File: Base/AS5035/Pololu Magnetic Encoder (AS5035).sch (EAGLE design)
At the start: 9 parts, among them U1 AS5035

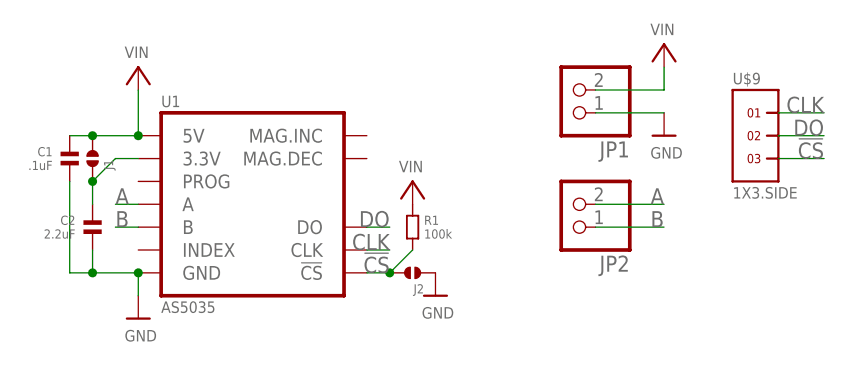
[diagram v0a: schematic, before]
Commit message: Cleaned up AS5035 based Magnetic Encoder. Added Silkscreen adn removed SPI components.
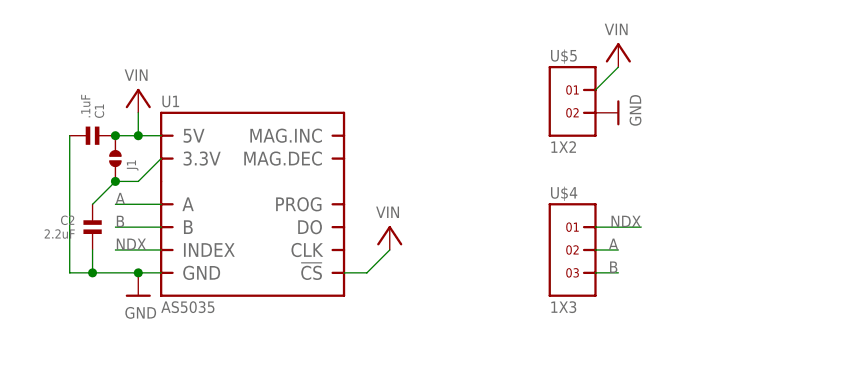
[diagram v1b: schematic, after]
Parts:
- removed J2: (no value), .solderjumper:SOLDERJUMPER.2.LRG.PASTE
- removed JP1, JP2: (no value), microbuilder:HEADER-1X2ROUND
- removed R1: 100k, .standardparts:RESISTOR.0603
- removed U$9: 1X3.SIDE, .standardheaders:1X3.SIDE
- added U$4: 1X3, headers(.1in):1X3
- added U$5: 1X2, headers(.1in):1X2
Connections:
- removed net !CS: J2.2, R1.2, U$9.3, U1.!CS
- removed net CLK: U$9.1, U1.CLK
- removed net DO: U$9.2, U1.DO
- new net NDX: U$4.1, U1.INDEX
- net A: now also U$4.2; no longer JP2.2
- net B: now also U$4.3; no longer JP2.1
- net GND: now also U$5.2; no longer J2.1, JP1.1
- net VIN: now also U$5.1, U1.!CS; no longer JP1.2, R1.1
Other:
- moved on the sheet: C1, J1
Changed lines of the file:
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@@
 <?xml version="1.0" encoding="utf-8"?>
 <!DOCTYPE eagle SYSTEM "eagle.dtd">
-<eagle version="6.3">
+<eagle version="6.4">
 <drawing>
 <settings>
@@
 <part name="U$2" library="microbuilder" deviceset="VIN" device=""/>
 <part name="U$3" library="microbuilder" deviceset="GND" device=""/>
-<part name="U$4" library="microbuilder" deviceset="GND" device=""/>
-<part name="J2" library=".solderjumper" deviceset="SOLDERJUMPER.2" device=".LRG.PASTE"/>
 <part name="U$7" library="microbuilder" deviceset="VIN" device=""/>
 <part name="U$8" library="microbuilder" deviceset="GND" device=""/>
-<part name="U$9" library=".standardheaders" deviceset="1X3" device=".SIDE"/>
 <part name="U$10" library="thinkmaketest" deviceset="A4_LAYOUT" device=""/>
-<part name="JP1" library="microbuilder" deviceset="HEADER-1X2" device="ROUND"/>
-<part name="JP2" library="microbuilder" deviceset="HEADER-1X2" device="ROUND"/>
-<part name="R1" library=".standardparts" deviceset="RESISTOR" device=".0603" value="100k"/>
 <part name="U$1" library="microbuilder" deviceset="VIN" device=""/>
+<part name="U$4" library="headers(.1in)" deviceset="1X3" device=""/>
+<part name="U$5" library="headers(.1in)" deviceset="1X2" device=""/>
 </parts>
 <sheets>
@@
 <instances>
 <instance part="U1" gate="G$1" x="38.1" y="142.24"/>
-<instance part="C1" gate="G$1" x="17.78" y="147.32" rot="MR270"/>
+<instance part="C1" gate="G$1" x="20.32" y="149.86" rot="MR0"/>
 <instance part="C2" gate="G$1" x="20.32" y="139.7" rot="MR270"/>
-<instance part="J1" gate="G$1" x="20.32" y="147.32" rot="MR90"/>
-<instance part="U$2" gate="G$1" x="25.4" y="154.94"/>
-<instance part="U$3" gate="G$1" x="25.4" y="129.54"/>
-<instance part="U$4" gate="G$1" x="58.42" y="132.08"/>
-<instance part="J2" gate="G$1" x="55.88" y="134.62" rot="R180"/>
-<instance part="U$7" gate="G$1" x="83.82" y="157.48"/>
-<instance part="U$8" gate="G$1" x="83.82" y="149.86"/>
-<instance part="U$9" gate="G$1" x="93.98" y="149.86"/>
+<instance part="J1" gate="G$1" x="22.86" y="147.32" rot="MR90"/>
+<instance part="U$2" gate="G$1" x="25.4" y="152.4"/>
+<instance part="U$3" gate="G$1" x="25.4" y="132.08"/>
+<instance part="U$7" gate="G$1" x="78.74" y="157.48"/>
+<instance part="U$8" gate="G$1" x="78.74" y="152.4" rot="R90"/>
 <instance part="U$10" gate="G$1" x="0" y="0"/>
-<instance part="JP1" gate="G$1" x="73.66" y="154.94" rot="R180"/>
-<instance part="JP2" gate="G$1" x="73.66" y="142.24" rot="R180"/>
-<instance part="R1" gate="G$1" x="55.88" y="139.7" rot="R270"/>
-<instance part="U$1" gate="G$1" x="55.88" y="142.24"/>
+<instance part="U$1" gate="G$1" x="53.34" y="137.16"/>
+<instance part="U$4" gate="G$1" x="73.66" y="137.16"/>
+<instance part="U$5" gate="G$1" x="73.66" y="154.94"/>
 </instances>
 <busses>
@@
 <pinref part="U1" gate="G$1" pin="5V"/>
 <pinref part="U$2" gate="G$1" pin="VIN"/>
-<wire x1="25.4" y1="149.86" x2="25.4" y2="154.94" width="0.1524" layer="91"/>
 <pinref part="C1" gate="G$1" pin="1"/>
+<pinref part="J1" gate="G$1" pin="2"/>
+<wire x1="22.86" y1="149.86" x2="25.4" y2="149.86" width="0.1524" layer="91"/>
+<junction x="22.86" y="149.86"/>
+<wire x1="25.4" y1="149.86" x2="27.94" y2="149.86" width="0.1524" layer="91"/>
+<wire x1="25.4" y1="149.86" x2="25.4" y2="152.4" width="0.1524" layer="91"/>
 <junction x="25.4" y="149.86"/>
-<wire x1="17.78" y1="149.86" x2="20.32" y2="149.86" width="0.1524" layer="91"/>
-<pinref part="J1" gate="G$1" pin="2"/>
-<wire x1="20.32" y1="149.86" x2="25.4" y2="149.86" width="0.1524" layer="91"/>
-<junction x="20.32" y="149.86"/>
 </segment>
 <segment>
 <pinref part="U$7" gate="G$1" pin="VIN"/>
-<wire x1="83.82" y1="154.94" x2="83.82" y2="157.48" width="0.1524" layer="91"/>
-<pinref part="JP1" gate="G$1" pin="2"/>
-<wire x1="76.2" y1="154.94" x2="83.82" y2="154.94" width="0.1524" layer="91"/>
-</segment>
-<segment>
-<pinref part="R1" gate="G$1" pin="1"/>
+<wire x1="76.2" y1="154.94" x2="78.74" y2="157.48" width="0.1524" layer="91"/>
+<pinref part="U$5" gate="G$1" pin="1"/>
+</segment>
+<segment>
+<pinref part="U1" gate="G$1" pin="!CS"/>
 <pinref part="U$1" gate="G$1" pin="VIN"/>
+<wire x1="48.26" y1="134.62" x2="50.8" y2="134.62" width="0.1524" layer="91"/>
+<wire x1="50.8" y1="134.62" x2="53.34" y2="137.16" width="0.1524" layer="91"/>
 </segment>
 </net>
@@
 <segment>
 <pinref part="U1" gate="G$1" pin="A"/>
-<wire x1="25.4" y1="142.24" x2="22.86" y2="142.24" width="0.1524" layer="91"/>
-<label x="22.86" y="142.24" size="1.778" layer="95"/>
-</segment>
-<segment>
-<pinref part="JP2" gate="G$1" pin="2"/>
-<wire x1="76.2" y1="142.24" x2="83.82" y2="142.24" width="0.1524" layer="91"/>
-<label x="83.82" y="142.24" size="1.778" layer="95" rot="MR0"/>
+<wire x1="27.94" y1="142.24" x2="22.86" y2="142.24" width="0.1524" layer="91"/>
+<label x="22.86" y="142.24" size="1.27" layer="95"/>
+</segment>
+<segment>
+<pinref part="U$4" gate="G$1" pin="2"/>
+<wire x1="78.74" y1="137.16" x2="76.2" y2="137.16" width="0.1524" layer="91"/>
+<label x="78.74" y="137.16" size="1.27" layer="95" rot="MR0"/>
 </segment>
 </net>
@@
 <segment>
 <pinref part="U1" gate="G$1" pin="B"/>
-<wire x1="22.86" y1="139.7" x2="25.4" y2="139.7" width="0.1524" layer="91"/>
-<label x="22.86" y="139.7" size="1.778" layer="95"/>
-</segment>
-<segment>
-<pinref part="JP2" gate="G$1" pin="1"/>
-<wire x1="83.82" y1="139.7" x2="76.2" y2="139.7" width="0.1524" layer="91"/>
-<label x="83.82" y="139.7" size="1.778" layer="95" rot="MR0"/>
+<wire x1="22.86" y1="139.7" x2="27.94" y2="139.7" width="0.1524" layer="91"/>
+<label x="22.86" y="139.7" size="1.27" layer="95"/>
+</segment>
+<segment>
+<pinref part="U$4" gate="G$1" pin="3"/>
+<wire x1="76.2" y1="134.62" x2="78.74" y2="134.62" width="0.1524" layer="91"/>
+<label x="78.74" y="134.62" size="1.27" layer="95" rot="MR0"/>
 </segment>
 </net>
@@
 <pinref part="U$3" gate="G$1" pin="GND"/>
 <pinref part="U1" gate="G$1" pin="GND"/>
-<wire x1="25.4" y1="132.08" x2="25.4" y2="134.62" width="0.1524" layer="91"/>
+<wire x1="27.94" y1="134.62" x2="25.4" y2="134.62" width="0.1524" layer="91"/>
+<pinref part="C2" gate="G$1" pin="2"/>
 <wire x1="25.4" y1="134.62" x2="20.32" y2="134.62" width="0.1524" layer="91"/>
-<junction x="25.4" y="134.62"/>
-<pinref part="C2" gate="G$1" pin="2"/>
 <wire x1="20.32" y1="134.62" x2="20.32" y2="137.16" width="0.1524" layer="91"/>
 <pinref part="C1" gate="G$1" pin="2"/>
-<wire x1="17.78" y1="144.78" x2="17.78" y2="134.62" width="0.1524" layer="91"/>
+<wire x1="17.78" y1="149.86" x2="17.78" y2="134.62" width="0.1524" layer="91"/>
 <wire x1="17.78" y1="134.62" x2="20.32" y2="134.62" width="0.1524" layer="91"/>
 <junction x="20.32" y="134.62"/>
-</segment>
-<segment>
-<pinref part="JP1" gate="G$1" pin="1"/>
-<wire x1="83.82" y1="152.4" x2="76.2" y2="152.4" width="0.1524" layer="91"/>
+<junction x="25.4" y="134.62"/>
+</segment>
+<segment>
 <pinref part="U$8" gate="G$1" pin="GND"/>
-</segment>
-<segment>
-<pinref part="J2" gate="G$1" pin="1"/>
-<pinref part="U$4" gate="G$1" pin="GND"/>
-</segment>
-</net>
-<net name="!CS" class="0">
-<segment>
-<pinref part="U$9" gate="G$1" pin="3"/>
-<wire x1="96.52" y1="147.32" x2="101.6" y2="147.32" width="0.1524" layer="91"/>
-<label x="101.6" y="147.32" size="1.778" layer="95" rot="MR0"/>
-</segment>
-<segment>
-<pinref part="J2" gate="G$1" pin="2"/>
-<pinref part="U1" gate="G$1" pin="!CS"/>
-<wire x1="53.34" y1="134.62" x2="50.8" y2="134.62" width="0.1524" layer="91"/>
-<wire x1="53.34" y1="134.62" x2="55.88" y2="137.16" width="0.1524" layer="91"/>
-<junction x="53.34" y="134.62"/>
-<pinref part="R1" gate="G$1" pin="2"/>
-<label x="53.34" y="134.62" size="1.778" layer="95" rot="MR0"/>
-</segment>
-</net>
-<net name="CLK" class="0">
-<segment>
-<pinref part="U1" gate="G$1" pin="CLK"/>
-<wire x1="50.8" y1="137.16" x2="53.34" y2="137.16" width="0.1524" layer="91"/>
-<label x="53.34" y="137.16" size="1.778" layer="95" rot="MR0"/>
-</segment>
-<segment>
-<pinref part="U$9" gate="G$1" pin="1"/>
-<wire x1="96.52" y1="152.4" x2="101.6" y2="152.4" width="0.1524" layer="91"/>
-<label x="101.6" y="152.4" size="1.778" layer="95" rot="MR0"/>
-</segment>
-</net>
-<net name="DO" class="0">
-<segment>
-<pinref part="U1" gate="G$1" pin="DO"/>
-<wire x1="50.8" y1="139.7" x2="53.34" y2="139.7" width="0.1524" layer="91"/>
-<label x="53.34" y="139.7" size="1.778" layer="95" rot="MR0"/>
-</segment>
-<segment>
-<pinref part="U$9" gate="G$1" pin="2"/>
-<wire x1="96.52" y1="149.86" x2="101.6" y2="149.86" width="0.1524" layer="91"/>
-<label x="101.6" y="149.86" size="1.778" layer="95" rot="MR0"/>
+<pinref part="U$5" gate="G$1" pin="2"/>
 </segment>
 </net>
@@
 <pinref part="C2" gate="G$1" pin="1"/>
 <pinref part="J1" gate="G$1" pin="1"/>
-<wire x1="20.32" y1="144.78" x2="20.32" y2="142.24" width="0.1524" layer="91"/>
+<wire x1="22.86" y1="144.78" x2="20.32" y2="142.24" width="0.1524" layer="91"/>
 <pinref part="U1" gate="G$1" pin="3.3V"/>
-<wire x1="20.32" y1="144.78" x2="22.86" y2="147.32" width="0.1524" layer="91"/>
-<wire x1="22.86" y1="147.32" x2="25.4" y2="147.32" width="0.1524" layer="91"/>
-<junction x="20.32" y="144.78"/>
-</segment>
-</net>
+<wire x1="22.86" y1="144.78" x2="25.4" y2="144.78" width="0.1524" layer="91"/>
+<wire x1="25.4" y1="144.78" x2="27.94" y2="147.32" width="0.1524" layer="91"/>
+<junction x="22.86" y="144.78"/>
+</segment>
+</net>
+<net name="NDX" class="0">
+<segment>
+<pinref part="U1" gate="G$1" pin="INDEX"/>
+<wire x1="27.94" y1="137.16" x2="22.86" y2="137.16" width="0.1524" layer="91"/>
+<label x="22.86" y="137.16" size="1.27" layer="95"/>
+</segment>
+<segment>
+<pinref part="U$4" gate="G$1" pin="1"/>
+<wire x1="76.2" y1="139.7" x2="81.28" y2="139.7" width="0.1524" layer="91"/>
+<label x="81.28" y="139.7" size="1.27" layer="95" rot="MR0"/>
+</segment>
+</net>

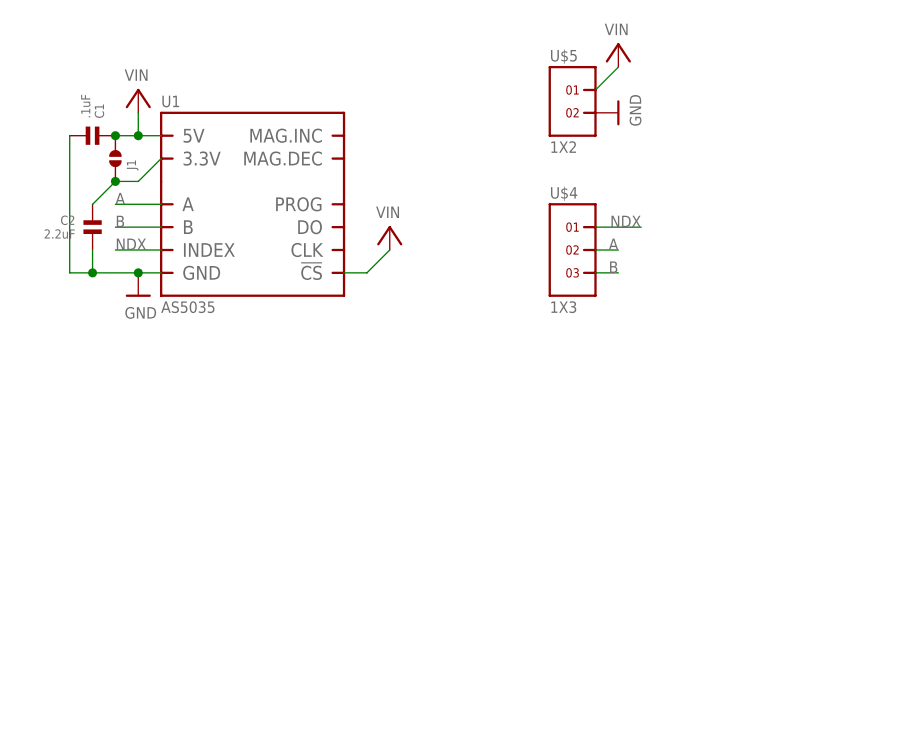
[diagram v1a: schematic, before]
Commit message: CS should be tied low for QEI to work on the AS5035
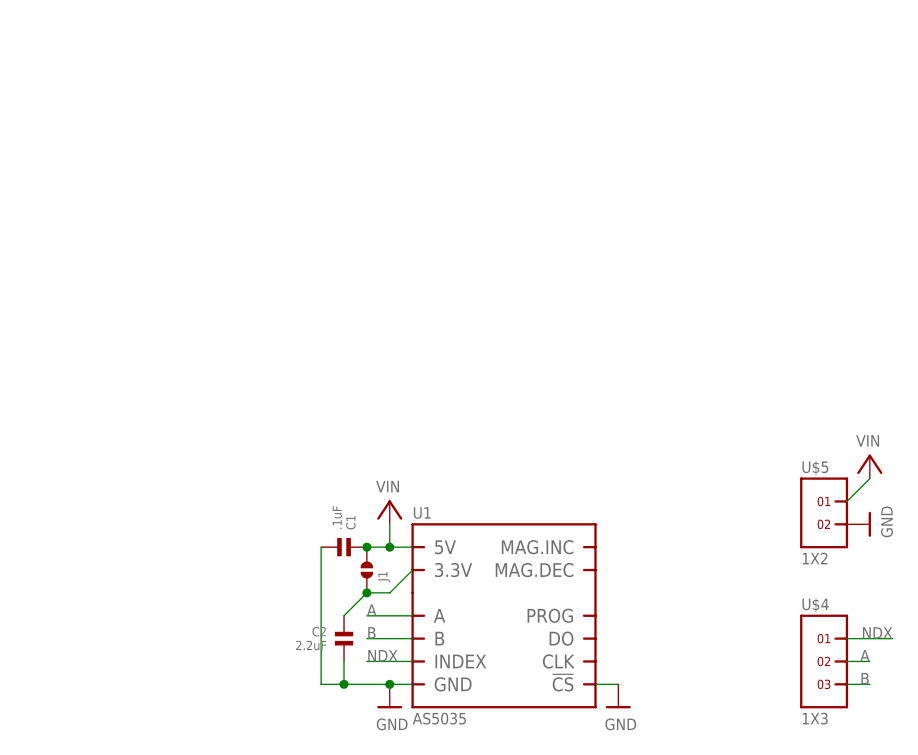
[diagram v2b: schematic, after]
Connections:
- net GND: now also U1.!CS
- net VIN: no longer U1.!CS
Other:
- moved on the sheet: C1, C2, J1, U$4, U$5, U1
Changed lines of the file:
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@@
 <part name="U$8" library="microbuilder" deviceset="GND" device=""/>
 <part name="U$10" library="thinkmaketest" deviceset="A4_LAYOUT" device=""/>
-<part name="U$1" library="microbuilder" deviceset="VIN" device=""/>
 <part name="U$4" library="headers(.1in)" deviceset="1X3" device=""/>
 <part name="U$5" library="headers(.1in)" deviceset="1X2" device=""/>
+<part name="U$1" library="microbuilder" deviceset="GND" device=""/>
 </parts>
 <sheets>
@@
 </plain>
 <instances>
-<instance part="U1" gate="G$1" x="38.1" y="142.24"/>
-<instance part="C1" gate="G$1" x="20.32" y="149.86" rot="MR0"/>
-<instance part="C2" gate="G$1" x="20.32" y="139.7" rot="MR270"/>
-<instance part="J1" gate="G$1" x="22.86" y="147.32" rot="MR90"/>
-<instance part="U$2" gate="G$1" x="25.4" y="152.4"/>
-<instance part="U$3" gate="G$1" x="25.4" y="132.08"/>
-<instance part="U$7" gate="G$1" x="78.74" y="157.48"/>
-<instance part="U$8" gate="G$1" x="78.74" y="152.4" rot="R90"/>
+<instance part="U1" gate="G$1" x="66.04" y="96.52"/>
+<instance part="C1" gate="G$1" x="48.26" y="104.14" rot="MR0"/>
+<instance part="C2" gate="G$1" x="48.26" y="93.98" rot="MR270"/>
+<instance part="J1" gate="G$1" x="50.8" y="101.6" rot="MR90"/>
+<instance part="U$2" gate="G$1" x="53.34" y="106.68"/>
+<instance part="U$3" gate="G$1" x="53.34" y="86.36"/>
+<instance part="U$7" gate="G$1" x="106.68" y="111.76"/>
+<instance part="U$8" gate="G$1" x="106.68" y="106.68" rot="R90"/>
 <instance part="U$10" gate="G$1" x="0" y="0"/>
-<instance part="U$1" gate="G$1" x="53.34" y="137.16"/>
-<instance part="U$4" gate="G$1" x="73.66" y="137.16"/>
-<instance part="U$5" gate="G$1" x="73.66" y="154.94"/>
+<instance part="U$4" gate="G$1" x="101.6" y="91.44"/>
+<instance part="U$5" gate="G$1" x="101.6" y="109.22"/>
+<instance part="U$1" gate="G$1" x="78.74" y="86.36"/>
 </instances>
 <busses>
@@
 <pinref part="C1" gate="G$1" pin="1"/>
 <pinref part="J1" gate="G$1" pin="2"/>
-<wire x1="22.86" y1="149.86" x2="25.4" y2="149.86" width="0.1524" layer="91"/>
-<junction x="22.86" y="149.86"/>
-<wire x1="25.4" y1="149.86" x2="27.94" y2="149.86" width="0.1524" layer="91"/>
-<wire x1="25.4" y1="149.86" x2="25.4" y2="152.4" width="0.1524" layer="91"/>
-<junction x="25.4" y="149.86"/>
+<wire x1="50.8" y1="104.14" x2="53.34" y2="104.14" width="0.1524" layer="91"/>
+<junction x="50.8" y="104.14"/>
+<wire x1="53.34" y1="104.14" x2="55.88" y2="104.14" width="0.1524" layer="91"/>
+<wire x1="53.34" y1="104.14" x2="53.34" y2="106.68" width="0.1524" layer="91"/>
+<junction x="53.34" y="104.14"/>
 </segment>
 <segment>
 <pinref part="U$7" gate="G$1" pin="VIN"/>
-<wire x1="76.2" y1="154.94" x2="78.74" y2="157.48" width="0.1524" layer="91"/>
+<wire x1="104.14" y1="109.22" x2="106.68" y2="111.76" width="0.1524" layer="91"/>
 <pinref part="U$5" gate="G$1" pin="1"/>
-</segment>
-<segment>
-<pinref part="U1" gate="G$1" pin="!CS"/>
-<pinref part="U$1" gate="G$1" pin="VIN"/>
-<wire x1="48.26" y1="134.62" x2="50.8" y2="134.62" width="0.1524" layer="91"/>
-<wire x1="50.8" y1="134.62" x2="53.34" y2="137.16" width="0.1524" layer="91"/>
 </segment>
 </net>
@@
 <segment>
 <pinref part="U1" gate="G$1" pin="A"/>
-<wire x1="27.94" y1="142.24" x2="22.86" y2="142.24" width="0.1524" layer="91"/>
-<label x="22.86" y="142.24" size="1.27" layer="95"/>
+<wire x1="55.88" y1="96.52" x2="50.8" y2="96.52" width="0.1524" layer="91"/>
+<label x="50.8" y="96.52" size="1.27" layer="95"/>
 </segment>
 <segment>
 <pinref part="U$4" gate="G$1" pin="2"/>
-<wire x1="78.74" y1="137.16" x2="76.2" y2="137.16" width="0.1524" layer="91"/>
-<label x="78.74" y="137.16" size="1.27" layer="95" rot="MR0"/>
+<wire x1="106.68" y1="91.44" x2="104.14" y2="91.44" width="0.1524" layer="91"/>
+<label x="106.68" y="91.44" size="1.27" layer="95" rot="MR0"/>
 </segment>
 </net>
@@
 <segment>
 <pinref part="U1" gate="G$1" pin="B"/>
-<wire x1="22.86" y1="139.7" x2="27.94" y2="139.7" width="0.1524" layer="91"/>
-<label x="22.86" y="139.7" size="1.27" layer="95"/>
+<wire x1="50.8" y1="93.98" x2="55.88" y2="93.98" width="0.1524" layer="91"/>
+<label x="50.8" y="93.98" size="1.27" layer="95"/>
 </segment>
 <segment>
 <pinref part="U$4" gate="G$1" pin="3"/>
-<wire x1="76.2" y1="134.62" x2="78.74" y2="134.62" width="0.1524" layer="91"/>
-<label x="78.74" y="134.62" size="1.27" layer="95" rot="MR0"/>
+<wire x1="104.14" y1="88.9" x2="106.68" y2="88.9" width="0.1524" layer="91"/>
+<label x="106.68" y="88.9" size="1.27" layer="95" rot="MR0"/>
 </segment>
 </net>
@@
 <pinref part="U$3" gate="G$1" pin="GND"/>
 <pinref part="U1" gate="G$1" pin="GND"/>
-<wire x1="27.94" y1="134.62" x2="25.4" y2="134.62" width="0.1524" layer="91"/>
+<wire x1="55.88" y1="88.9" x2="53.34" y2="88.9" width="0.1524" layer="91"/>
 <pinref part="C2" gate="G$1" pin="2"/>
-<wire x1="25.4" y1="134.62" x2="20.32" y2="134.62" width="0.1524" layer="91"/>
-<wire x1="20.32" y1="134.62" x2="20.32" y2="137.16" width="0.1524" layer="91"/>
+<wire x1="53.34" y1="88.9" x2="48.26" y2="88.9" width="0.1524" layer="91"/>
+<wire x1="48.26" y1="88.9" x2="48.26" y2="91.44" width="0.1524" layer="91"/>
 <pinref part="C1" gate="G$1" pin="2"/>
-<wire x1="17.78" y1="149.86" x2="17.78" y2="134.62" width="0.1524" layer="91"/>
-<wire x1="17.78" y1="134.62" x2="20.32" y2="134.62" width="0.1524" layer="91"/>
-<junction x="20.32" y="134.62"/>
-<junction x="25.4" y="134.62"/>
+<wire x1="45.72" y1="104.14" x2="45.72" y2="88.9" width="0.1524" layer="91"/>
+<wire x1="45.72" y1="88.9" x2="48.26" y2="88.9" width="0.1524" layer="91"/>
+<junction x="48.26" y="88.9"/>
+<junction x="53.34" y="88.9"/>
 </segment>
 <segment>
 <pinref part="U$8" gate="G$1" pin="GND"/>
 <pinref part="U$5" gate="G$1" pin="2"/>
+</segment>
+<segment>
+<pinref part="U1" gate="G$1" pin="!CS"/>
+<wire x1="76.2" y1="88.9" x2="78.74" y2="88.9" width="0.1524" layer="91"/>
+<pinref part="U$1" gate="G$1" pin="GND"/>
 </segment>
 </net>
@@
 <pinref part="C2" gate="G$1" pin="1"/>
 <pinref part="J1" gate="G$1" pin="1"/>
-<wire x1="22.86" y1="144.78" x2="20.32" y2="142.24" width="0.1524" layer="91"/>
+<wire x1="50.8" y1="99.06" x2="48.26" y2="96.52" width="0.1524" layer="91"/>
 <pinref part="U1" gate="G$1" pin="3.3V"/>
-<wire x1="22.86" y1="144.78" x2="25.4" y2="144.78" width="0.1524" layer="91"/>
-<wire x1="25.4" y1="144.78" x2="27.94" y2="147.32" width="0.1524" layer="91"/>
-<junction x="22.86" y="144.78"/>
+<wire x1="50.8" y1="99.06" x2="53.34" y2="99.06" width="0.1524" layer="91"/>
+<wire x1="53.34" y1="99.06" x2="55.88" y2="101.6" width="0.1524" layer="91"/>
+<junction x="50.8" y="99.06"/>
 </segment>
 </net>
@@
 <segment>
 <pinref part="U1" gate="G$1" pin="INDEX"/>
-<wire x1="27.94" y1="137.16" x2="22.86" y2="137.16" width="0.1524" layer="91"/>
-<label x="22.86" y="137.16" size="1.27" layer="95"/>
+<wire x1="55.88" y1="91.44" x2="50.8" y2="91.44" width="0.1524" layer="91"/>
+<label x="50.8" y="91.44" size="1.27" layer="95"/>
 </segment>
 <segment>
 <pinref part="U$4" gate="G$1" pin="1"/>
-<wire x1="76.2" y1="139.7" x2="81.28" y2="139.7" width="0.1524" layer="91"/>
-<label x="81.28" y="139.7" size="1.27" layer="95" rot="MR0"/>
+<wire x1="104.14" y1="93.98" x2="109.22" y2="93.98" width="0.1524" layer="91"/>
+<label x="109.22" y="93.98" size="1.27" layer="95" rot="MR0"/>
 </segment>
 </net>
